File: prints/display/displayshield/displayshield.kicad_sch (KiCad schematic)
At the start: 9 parts, among them J1 Conn_01x16, J2 Screw_Terminal_01x11, SW1 SW_Push

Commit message: added new Printfiles for Displayshield and Measurements for second stack
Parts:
- added ADS1015: ~, ADAFRUIT:ADS1015, symbol ADAFRUIT:ADS1015
- added J3: RaspberryPiADC, TerminalBlock_4Ucon:TerminalBlock_4Ucon_1x02_P3.50mm_Vertical, symbol Connector:Screw_Terminal_01x02
- added J4: CurrentSensor, TerminalBlock_4Ucon:TerminalBlock_4Ucon_1x03_P3.50mm_Vertical, symbol Connector:Screw_Terminal_01x03
- J1: value Conn_01x16 -> Display
- J2: value Screw_Terminal_01x11 -> RaspberryPiDisplay
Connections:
- net +5V: now also ADS1015.1 (VIN), J4.1 (Pin_1)
- net GND: now also ADS1015.2 (GND), J4.3 (Pin_3)
- new net: ADS1015.3 (SCL), J3.1 (Pin_1)
- new net: ADS1015.4 (SDA), J3.2 (Pin_2)
- new net: ADS1015.11 (A0), J4.2 (Pin_2)
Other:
- note added: "2.1"
- note removed: "1"
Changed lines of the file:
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@@
+    (stroke (width 0) (type default))
+  )
+  (wire (pts (xy 173.355 47.625) (xy 178.435 47.625))
     (stroke (width 0) (type default))
   )
@@
     (stroke (width 0) (type default))
   )
+  (wire (pts (xy 174.625 40.005) (xy 174.625 26.035))
+    (stroke (width 0) (type default))
+  )
+  (wire (pts (xy 158.75 42.545) (xy 178.435 42.545))
+    (stroke (width 0) (type default))
+  )
   (wire (pts (xy 98.425 26.035) (xy 98.425 68.58))
     (stroke (width 0) (type default))
@@
     (stroke (width 0) (type default))
   )
+  (wire (pts (xy 173.355 45.085) (xy 178.435 45.085))
+    (stroke (width 0) (type default))
+  )
   (wire (pts (xy 118.745 26.035) (xy 118.745 58.42))
     (stroke (width 0) (type default))
@@
     (stroke (width 0) (type default))
   )
+  (wire (pts (xy 222.885 52.705) (xy 222.885 59.69))
+    (stroke (width 0) (type default))
+  )
   (wire (pts (xy 116.205 26.035) (xy 116.205 55.88))
     (stroke (width 0) (type default))
   )
+  (wire (pts (xy 222.885 26.035) (xy 222.885 47.625))
+    (stroke (width 0) (type default))
+  )
   (wire (pts (xy 93.345 41.91) (xy 93.345 53.34))
     (stroke (width 0) (type default))
@@
     (stroke (width 0) (type default))
   )
+  (wire (pts (xy 193.675 50.165) (xy 222.885 50.165))
+    (stroke (width 0) (type default))
+  )
   (wire (pts (xy 78.105 108.585) (xy 90.805 108.585))
     (stroke (width 0) (type default))
@@
   )
   (wire (pts (xy 81.28 83.185) (xy 93.345 83.185))
+    (stroke (width 0) (type default))
+  )
+  (wire (pts (xy 178.435 40.005) (xy 174.625 40.005))
+    (stroke (width 0) (type default))
+  )
+  (wire (pts (xy 158.75 59.69) (xy 158.75 42.545))
     (stroke (width 0) (type default))
   )
@@
     (effects (font (size 1.27 1.27)) (justify left bottom))
   )
-  (text "1\n" (at 268.605 194.31 0)
+  (text "2.1\n" (at 268.605 194.31 0)
     (effects (font (size 1.27 1.27)) (justify left bottom))
   )
@@
         (path "/bed1ac43-676b-436d-ad6e-1a552717c319"
           (reference "#PWR02") (unit 1)
+        )
+      )
+    )
+  )
+  (symbol (lib_id "power:GND") (at 158.75 59.69 0) (unit 1)
+    (in_bom yes) (on_board yes) (dnp no) (fields_autoplaced)
+    (property "Reference" "#PWR06" (at 158.75 66.04 0)
+      (effects (font (size 1.27 1.27)) hide)
+    )
+    (property "Value" "GND" (at 158.75 64.135 0)
+      (effects (font (size 1.27 1.27)))
+    )
+    (property "Footprint" "" (at 158.75 59.69 0)
+      (effects (font (size 1.27 1.27)) hide)
+    )
+    (property "Datasheet" "" (at 158.75 59.69 0)
+      (effects (font (size 1.27 1.27)) hide)
+    )
+    (pin "1")
+    (instances
+      (project "displayshield"
+        (path "/bed1ac43-676b-436d-ad6e-1a552717c319"
+          (reference "#PWR06") (unit 1)
+        )
+      )
+    )
+  )
+  (symbol (lib_id "Connector:Screw_Terminal_01x02") (at 168.275 45.085 0) (mirror y) (unit 1)
+    (in_bom yes) (on_board yes) (dnp no)
+    (property "Reference" "J3" (at 169.545 52.705 0)
+      (effects (font (size 1.27 1.27)) (justify left))
+    )
+    (property "Value" "RaspberryPiADC" (at 174.625 50.165 0)
+      (effects (font (size 1.27 1.27)) (justify left))
+    )
+    (property "Footprint" "TerminalBlock_4Ucon:TerminalBlock_4Ucon_1x02_P3.50mm_Vertical" (at 168.275 45.085 0)
+      (effects (font (size 1.27 1.27)) hide)
+    )
+    (property "Datasheet" "~" (at 168.275 45.085 0)
+      (effects (font (size 1.27 1.27)) hide)
+    )
+    (pin "2")
+    (pin "1")
+    (instances
+      (project "displayshield"
+        (path "/bed1ac43-676b-436d-ad6e-1a552717c319"
+          (reference "J3") (unit 1)
+        )
+      )
+    )
+  )
+  (symbol (lib_id "Connector:Screw_Terminal_01x03") (at 227.965 50.165 0) (unit 1)
+    (in_bom yes) (on_board yes) (dnp no)
+    (property "Reference" "J4" (at 227.965 59.055 0)
+      (effects (font (size 1.27 1.27)))
+    )
+    (property "Value" "CurrentSensor" (at 227.965 56.515 0)
+      (effects (font (size 1.27 1.27)))
+    )
+    (property "Footprint" "TerminalBlock_4Ucon:TerminalBlock_4Ucon_1x03_P3.50mm_Vertical" (at 227.965 50.165 0)
+      (effects (font (size 1.27 1.27)) hide)
+    )
+    (property "Datasheet" "~" (at 227.965 50.165 0)
+      (effects (font (size 1.27 1.27)) hide)
+    )
+    (pin "1")
+    (pin "2")
+    (pin "3")
+    (instances
+      (project "displayshield"
+        (path "/bed1ac43-676b-436d-ad6e-1a552717c319"
+          (reference "J4") (unit 1)
         )
       )
@@
       (effects (font (size 1.27 1.27)))
     )
-    (property "Value" "Screw_Terminal_01x11" (at 27.94 80.01 0)
+    (property "Value" "RaspberryPiDisplay" (at 27.94 80.01 0)
       (effects (font (size 1.27 1.27)))
     )
@@
     )
   )
+  (symbol (lib_id "ADAFRUIT:ADS1015") (at 192.405 38.735 0) (unit 1)
+    (in_bom yes) (on_board yes) (dnp no) (fields_autoplaced)
+    (property "Reference" "ADS1015" (at 186.055 36.195 0)
+      (effects (font (size 1.27 1.27)))
+    )
+    (property "Value" "~" (at 192.405 38.735 0)
+      (effects (font (size 1.27 1.27)))
+    )
+    (property "Footprint" "ADAFRUIT:ADS1015" (at 192.405 38.735 0)
+      (effects (font (size 1.27 1.27)) hide)
+    )
+    (property "Datasheet" "" (at 192.405 38.735 0)
+      (effects (font (size 1.27 1.27)) hide)
+    )
+    (pin "4")
+    (pin "10")
+    (pin "12")
+    (pin "5")
+    (pin "6")
+    (pin "3")
+    (pin "8")
+    (pin "11")
+    (pin "7")
+    (pin "2")
+    (pin "1")
+    (pin "9")
+    (instances
+      (project "displayshield"
+        (path "/bed1ac43-676b-436d-ad6e-1a552717c319"
+          (reference "ADS1015") (unit 1)
+        )
+      )
+    )
+  )
   (symbol (lib_id "Device:LED") (at 75.565 116.84 180) (unit 1)
     (in_bom yes) (on_board yes) (dnp no)
@@
       (effects (font (size 1.27 1.27)) (justify left))
     )
-    (property "Value" "Conn_01x16" (at 86.995 26.67 0)
+    (property "Value" "Display" (at 86.995 26.67 0)
       (effects (font (size 1.27 1.27)) (justify left))
     )
@@
     )
   )
+  (symbol (lib_id "power:+5V") (at 222.885 26.035 0) (mirror y) (unit 1)
+    (in_bom yes) (on_board yes) (dnp no) (fields_autoplaced)
+    (property "Reference" "#PWR03" (at 222.885 29.845 0)
+      (effects (font (size 1.27 1.27)) hide)
+    )
+    (property "Value" "+5V" (at 222.885 20.955 0)
+      (effects (font (size 1.27 1.27)))
+    )
+    (property "Footprint" "" (at 222.885 26.035 0)
+      (effects (font (size 1.27 1.27)) hide)
+    )
+    (property "Datasheet" "" (at 222.885 26.035 0)
+      (effects (font (size 1.27 1.27)) hide)
+    )
+    (pin "1")
+    (instances
+      (project "displayshield"
+        (path "/bed1ac43-676b-436d-ad6e-1a552717c319"
+          (reference "#PWR03") (unit 1)
+        )
+      )
+    )
+  )
   (symbol (lib_id "Device:R_Potentiometer") (at 139.7 41.91 180) (unit 1)
     (in_bom yes) (on_board yes) (dnp no) (fields_autoplaced)
@@
     )
   )
+  (symbol (lib_id "power:+5V") (at 174.625 26.035 0) (unit 1)
+    (in_bom yes) (on_board yes) (dnp no) (fields_autoplaced)
+    (property "Reference" "#PWR04" (at 174.625 29.845 0)
+      (effects (font (size 1.27 1.27)) hide)
+    )
+    (property "Value" "+5V" (at 174.625 20.955 0)
+      (effects (font (size 1.27 1.27)))
+    )
+    (property "Footprint" "" (at 174.625 26.035 0)
+      (effects (font (size 1.27 1.27)) hide)
+    )
+    (property "Datasheet" "" (at 174.625 26.035 0)
+      (effects (font (size 1.27 1.27)) hide)
+    )
+    (pin "1")
+    (instances
+      (project "displayshield"
+        (path "/bed1ac43-676b-436d-ad6e-1a552717c319"
+          (reference "#PWR04") (unit 1)
+        )
+      )
+    )
+  )
   (symbol (lib_id "power:GND") (at 90.805 131.445 0) (unit 1)
     (in_bom yes) (on_board yes) (dnp no) (fields_autoplaced)
@@
         )
       )
+    )
+  )
+  (symbol (lib_id "power:GND") (at 222.885 59.69 0) (mirror y) (unit 1)
+    (in_bom yes) (on_board yes) (dnp no) (fields_autoplaced)
+    (property "Reference" "#PWR05" (at 222.885 66.04 0)
+      (effects (font (size 1.27 1.27)) hide)
+    )
+    (property "Value" "GND" (at 222.885 64.135 0)
+      (effects (font (size 1.27 1.27)))
+    )
+    (property "Footprint" "" (at 222.885 59.69 0)
+      (effects (font (size 1.27 1.27)) hide)
+    )
+    (property "Datasheet" "" (at 222.885 59.69 0)
+      (effects (font (size 1.27 1.27)) hide)
+    )
+    (pin "1")
+    (instances
+      (project "displayshield"
+        (path "/bed1ac43-676b-436d-ad6e-1a552717c319"
+          (reference "#PWR05") (unit 1)
+        )
+      )

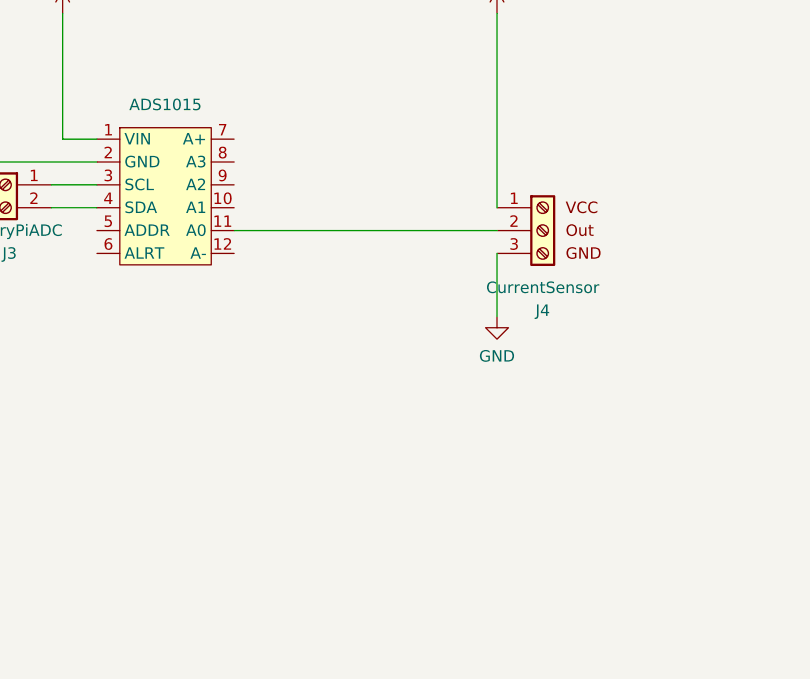
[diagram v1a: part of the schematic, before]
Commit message: Prints for Hallsensor
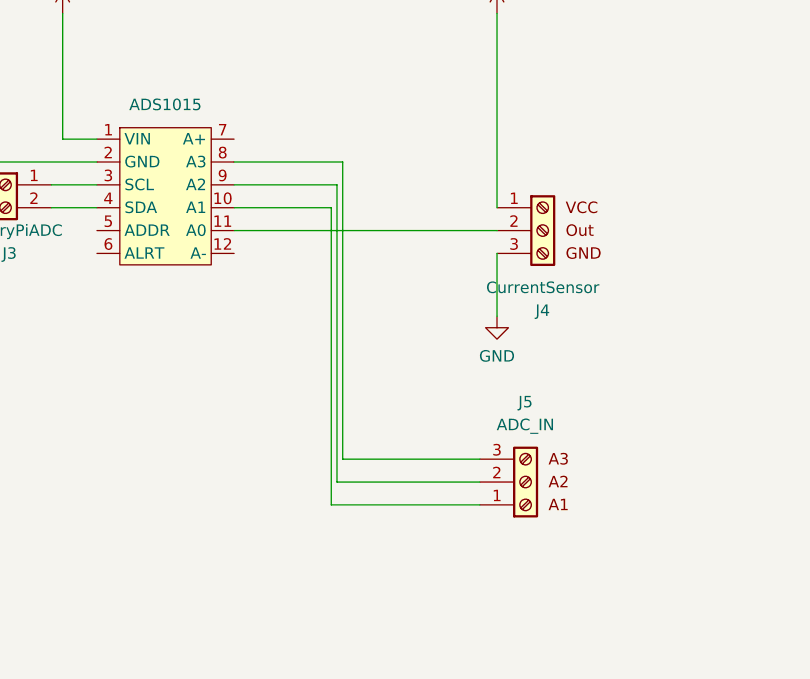
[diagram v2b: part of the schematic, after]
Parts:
- added J5: ADC_IN, TerminalBlock_4Ucon:TerminalBlock_4Ucon_1x03_P3.50mm_Vertical, symbol Connector:Screw_Terminal_01x03
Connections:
- net at ADS1015.10 (A1): now also J5.1 (Pin_1)
- net at ADS1015.8 (A3): now also J5.3 (Pin_3)
- net at ADS1015.9 (A2): now also J5.2 (Pin_2)
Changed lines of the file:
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@@
+    (stroke (width 0) (type default))
+  )
+  (wire (pts (xy 205.74 42.545) (xy 193.675 42.545))
     (stroke (width 0) (type default))
   )
@@
     (stroke (width 0) (type default))
   )
+  (wire (pts (xy 220.98 80.645) (xy 204.47 80.645))
+    (stroke (width 0) (type default))
+  )
   (wire (pts (xy 95.885 26.035) (xy 95.885 41.91))
     (stroke (width 0) (type default))
@@
     (stroke (width 0) (type default))
   )
+  (wire (pts (xy 205.74 75.565) (xy 205.74 42.545))
+    (stroke (width 0) (type default))
+  )
   (wire (pts (xy 93.345 38.1) (xy 139.7 38.1))
     (stroke (width 0) (type default))
@@
     (stroke (width 0) (type default))
   )
+  (wire (pts (xy 205.105 78.105) (xy 220.98 78.105))
+    (stroke (width 0) (type default))
+  )
   (wire (pts (xy 33.02 63.5) (xy 123.825 63.5))
     (stroke (width 0) (type default))
@@
     (stroke (width 0) (type default))
   )
+  (wire (pts (xy 204.47 80.645) (xy 204.47 47.625))
+    (stroke (width 0) (type default))
+  )
   (wire (pts (xy 64.135 116.84) (xy 71.755 116.84))
     (stroke (width 0) (type default))
@@
     (stroke (width 0) (type default))
   )
+  (wire (pts (xy 205.105 45.085) (xy 205.105 78.105))
+    (stroke (width 0) (type default))
+  )
   (wire (pts (xy 79.375 116.84) (xy 90.805 116.84))
     (stroke (width 0) (type default))
   )
+  (wire (pts (xy 204.47 47.625) (xy 193.675 47.625))
+    (stroke (width 0) (type default))
+  )
   (wire (pts (xy 33.02 66.04) (xy 103.505 66.04))
     (stroke (width 0) (type default))
@@
     (stroke (width 0) (type default))
   )
+  (wire (pts (xy 220.98 75.565) (xy 205.74 75.565))
+    (stroke (width 0) (type default))
+  )
   (wire (pts (xy 78.105 108.585) (xy 90.805 108.585))
     (stroke (width 0) (type default))
@@
   )
   (wire (pts (xy 64.135 76.2) (xy 33.02 76.2))
+    (stroke (width 0) (type default))
+  )
+  (wire (pts (xy 193.675 45.085) (xy 205.105 45.085))
     (stroke (width 0) (type default))
   )
@@
         )
       )
+    )
+  )
+  (symbol (lib_name "Screw_Terminal_01x03_1") (lib_id "Connector:Screw_Terminal_01x03") (at 226.06 78.105 0) (mirror x) (unit 1)
+    (in_bom yes) (on_board yes) (dnp no)
+    (property "Reference" "J5" (at 226.06 69.215 0)
+      (effects (font (size 1.27 1.27)))
+    )
+    (property "Value" "ADC_IN" (at 226.06 71.755 0)
+      (effects (font (size 1.27 1.27)))
+    )
+    (property "Footprint" "TerminalBlock_4Ucon:TerminalBlock_4Ucon_1x03_P3.50mm_Vertical" (at 226.06 78.105 0)
+      (effects (font (size 1.27 1.27)) hide)
+    )
+    (property "Datasheet" "~" (at 226.06 78.105 0)
+      (effects (font (size 1.27 1.27)) hide)
+    )
+    (pin "1")
+    (pin "2")
+    (pin "3")
+    (instances
+      (project "displayshield"
+        (path "/bed1ac43-676b-436d-ad6e-1a552717c319"
+          (reference "J5") (unit 1)
+        )
+      )
